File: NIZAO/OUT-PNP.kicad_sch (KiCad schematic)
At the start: 5 parts, among them U17 BTS723GWXUMA1

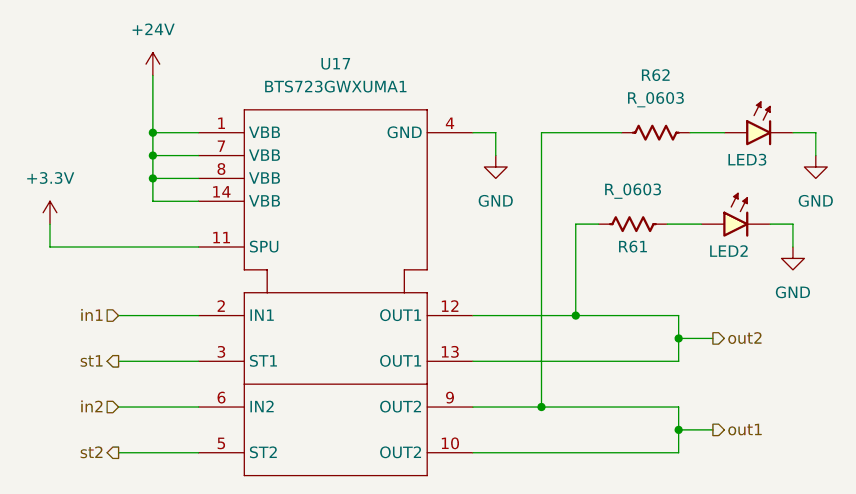
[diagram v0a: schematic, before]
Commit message: Colocandos los 3d de los componetes en la placa NIZAO
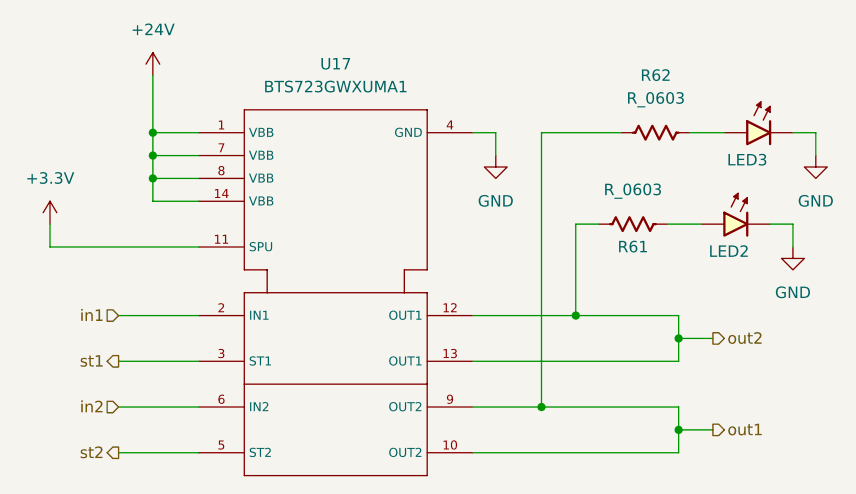
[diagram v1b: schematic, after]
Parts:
- U17: footprint Infineon BTS723GW:SOIC-14_L8.7-W3.9-P1.27-LS6.0-BL -> JLCImport:BTS723GWXUMA1; symbol EasyEDA:BTS723GWXUMA1 -> lcsc_imported:BTS723GWXUMA1; LCSC (none) -> C67625; Manufacturer (none) -> Infineon(英飞凌)
